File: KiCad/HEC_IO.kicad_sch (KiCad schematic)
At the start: 0 parts

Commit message: Add HEC Bus
The HEC bus packs a lot of information into a small amount of pins. It is suitable for cards with various complexity.
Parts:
- added BUS1, BUS2: ~, symbol New_Library:Bus_HEC
- added BUS3, BUS4: ~, symbol New_Library:Bus_HEC_5Vonly

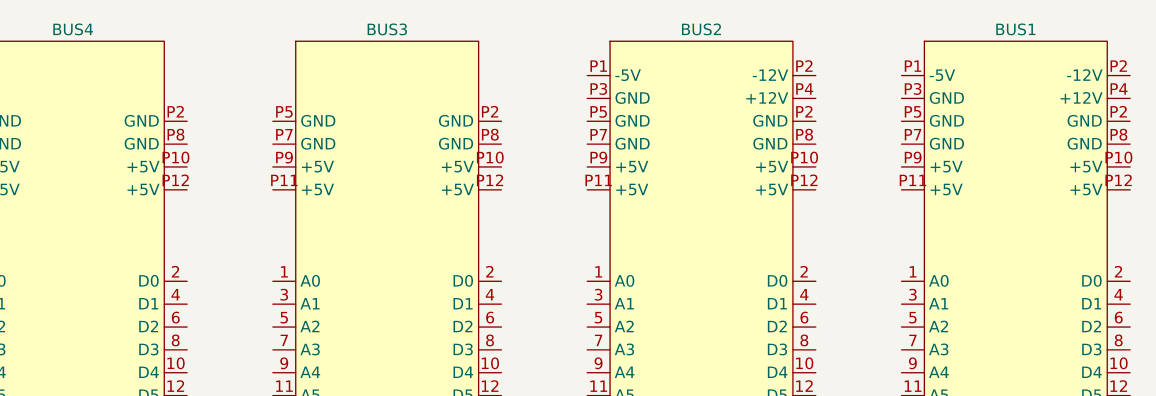
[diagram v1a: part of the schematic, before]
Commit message: Created footprint for HEC bus
Created footprints for HEC bus and some other updates.
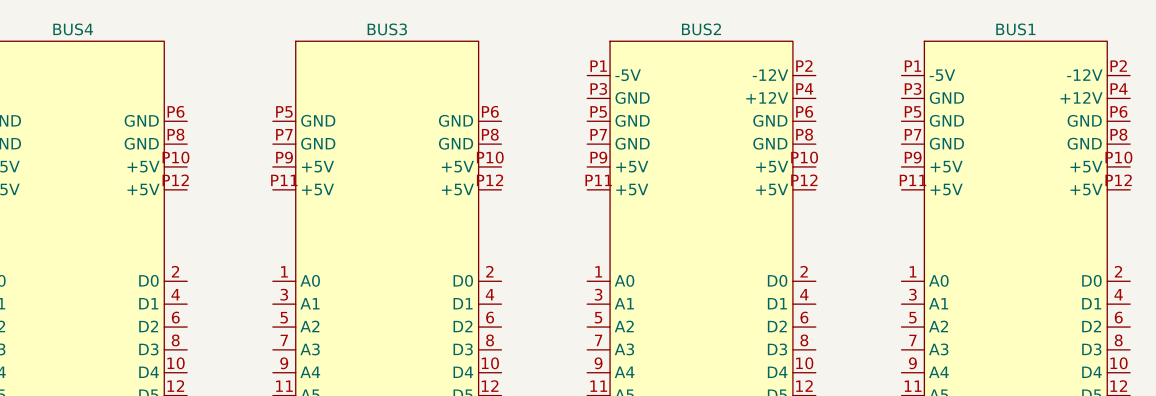
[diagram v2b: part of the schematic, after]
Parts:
- BUS1, BUS2: footprint (none) -> Library:Bus_HEC
- BUS3, BUS4: footprint (none) -> Library:Bus_HEC_5Vonly
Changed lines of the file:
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@@
       (effects (font (size 1.27 1.27)))
     )
-    (property "Footprint" "" (at 104.775 68.58 0)
+    (property "Footprint" "Library:Bus_HEC" (at 104.775 68.58 0)
       (effects (font (size 1.27 1.27)) hide)
     )
@@
     (pin "P11")
     (pin "P12")
-    (pin "P2")
     (pin "P2")
     (pin "P3")
     (pin "P4")
     (pin "P5")
+    (pin "P6")
     (pin "P7")
     (pin "P8")
@@
       (effects (font (size 1.27 1.27)))
     )
-    (property "Footprint" "" (at 34.925 68.58 0)
+    (property "Footprint" "Library:Bus_HEC_5Vonly" (at 34.925 68.58 0)
       (effects (font (size 1.27 1.27)) hide)
     )
@@
     (pin "P11")
     (pin "P12")
-    (pin "P2")
-    (pin "P5")
+    (pin "P5")
+    (pin "P6")
     (pin "P7")
     (pin "P8")
@@
     )
   )
-  (symbol (lib_id "New_Library:Bus_HEC_5Vonly") (at 69.85 68.58 0) (unit 1)
+  (symbol (lib_name "Bus_HEC_5Vonly_1") (lib_id "New_Library:Bus_HEC_5Vonly") (at 69.85 68.58 0) (unit 1)
     (in_bom yes) (on_board yes) (dnp no) (fields_autoplaced)
     (property "Reference" "BUS3" (at 69.85 30.48 0)
@@
       (effects (font (size 1.27 1.27)))
     )
-    (property "Footprint" "" (at 69.85 68.58 0)
+    (property "Footprint" "Library:Bus_HEC_5Vonly" (at 69.85 68.58 0)
       (effects (font (size 1.27 1.27)) hide)
     )
@@
     (pin "P11")
     (pin "P12")
-    (pin "P2")
-    (pin "P5")
+    (pin "P5")
+    (pin "P6")
     (pin "P7")
     (pin "P8")
@@
     )
   )
-  (symbol (lib_id "New_Library:Bus_HEC") (at 139.7 68.58 0) (unit 1)
+  (symbol (lib_name "Bus_HEC_1") (lib_id "New_Library:Bus_HEC") (at 139.7 68.58 0) (unit 1)
     (in_bom yes) (on_board yes) (dnp no) (fields_autoplaced)
     (property "Reference" "BUS1" (at 139.7 30.48 0)
@@
       (effects (font (size 1.27 1.27)))
     )
-    (property "Footprint" "" (at 139.7 68.58 0)
+    (property "Footprint" "Library:Bus_HEC" (at 139.7 68.58 0)
       (effects (font (size 1.27 1.27)) hide)
     )
@@
     (pin "P11")
     (pin "P12")
-    (pin "P2")
     (pin "P2")
     (pin "P3")
     (pin "P4")
     (pin "P5")
-    (pin "P7")
-    (pin "P8")
+    (pin "P6")
+    (pin "P7")
+    (pin "P8")

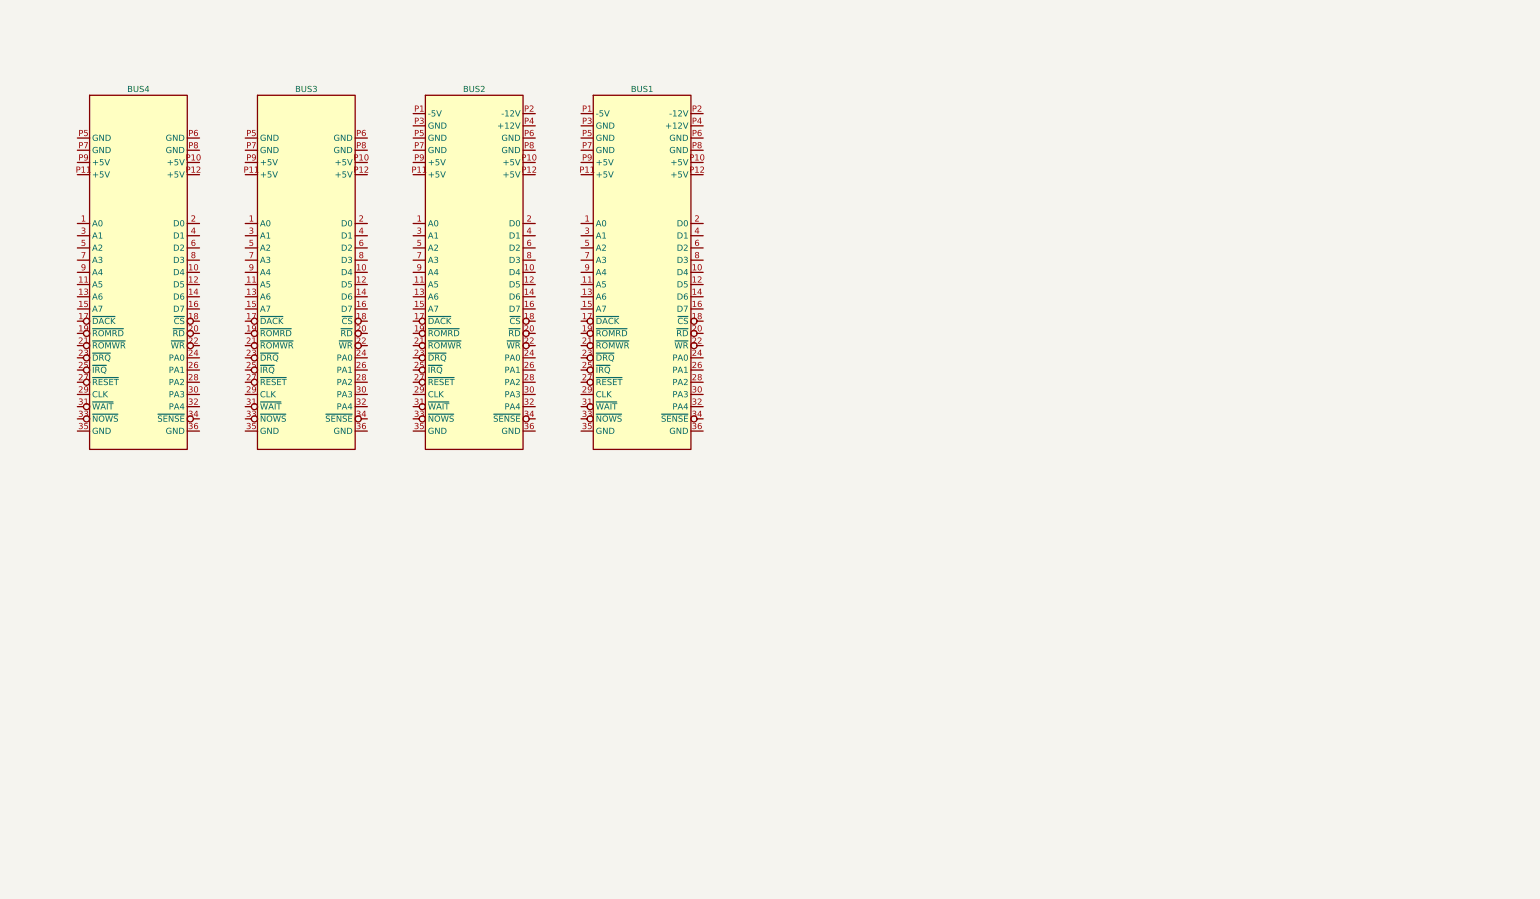
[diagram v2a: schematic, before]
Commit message: IO implementation
Implemented most of IO functions, add connections between the schematics.
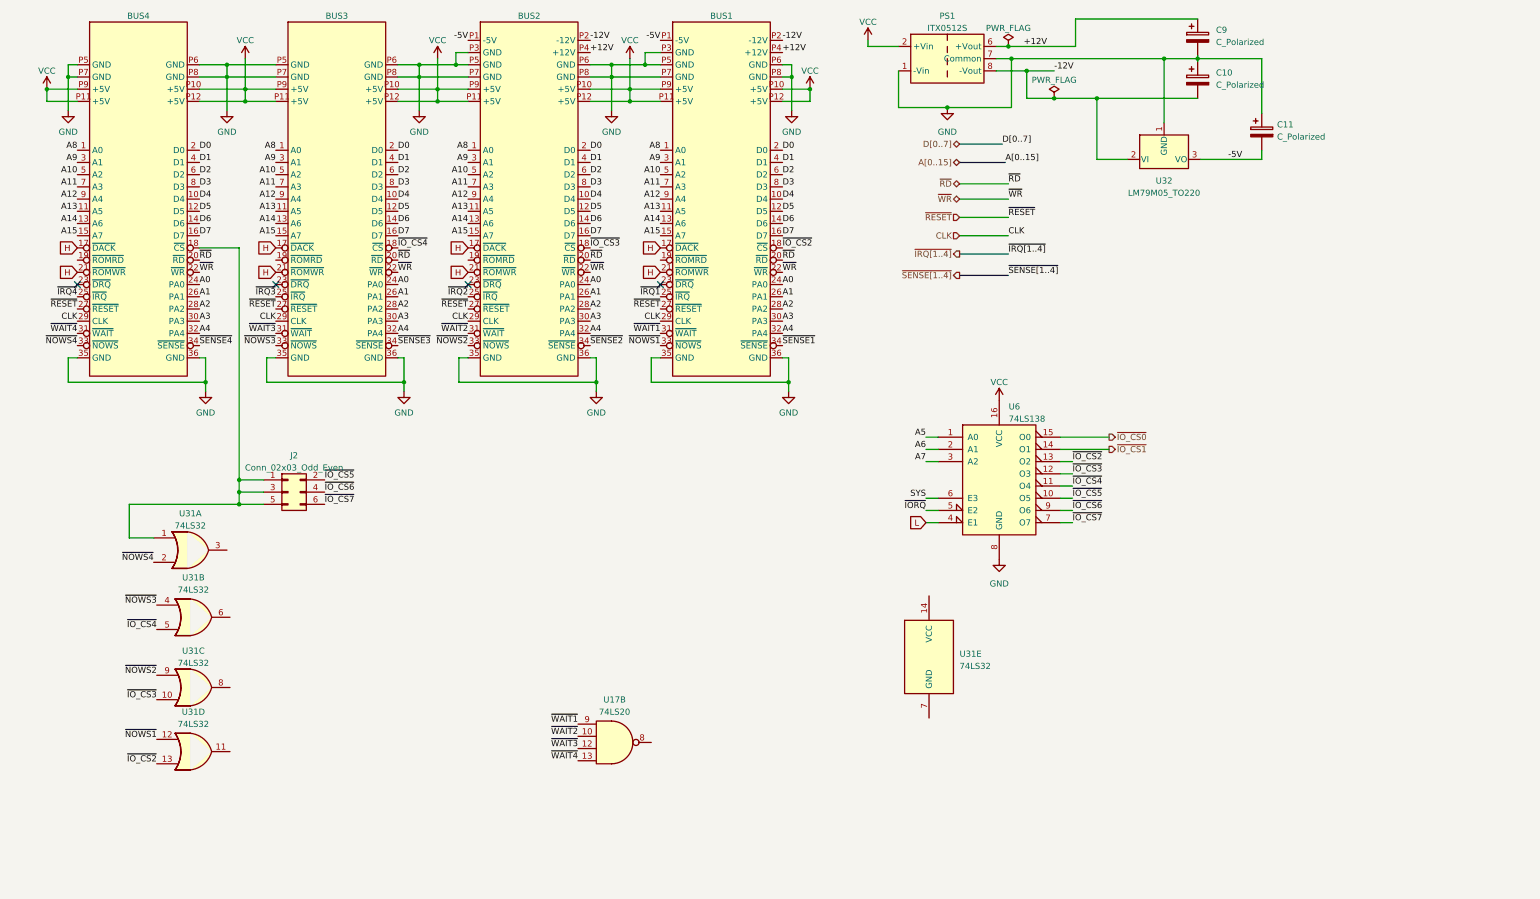
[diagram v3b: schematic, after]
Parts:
- added C10, C11, C9: C_Polarized, symbol Device:C_Polarized
- added J2: Conn_02x03_Odd_Even, symbol Connector_Generic:Conn_02x03_Odd_Even
- added PS1: ITX0512S, Converter_DCDC:Converter_DCDC_XP_POWER-ITxxxxxS_THT, symbol Converter_DCDC:ITX0512S
- added U17: 74LS20, symbol 74xx:74LS20
- added U31: 74LS32, symbol 74xx:74LS32
- added U32: LM79M05_TO220, Package_TO_SOT_THT:TO-92_Inline, symbol Regulator_Linear:LM79M05_TO220
- added U6: 74LS138, Package_DIP:DIP-16_W7.62mm_Socket, symbol 74xx:74LS138
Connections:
- net A8: now reaches BUS2.1 (A0)
- net A8: now also BUS1.1 (A0), BUS3.1 (A0), BUS4.1 (A0)
- net D4: now reaches BUS2.10 (D4)
- net D4: now also BUS1.10 (D4), BUS3.10 (D4), BUS4.10 (D4)
- net A13: now reaches BUS2.11 (A5)
- net A13: now also BUS1.11 (A5), BUS3.11 (A5), BUS4.11 (A5)
- net D5: now reaches BUS2.12 (D5)
- net D5: now also BUS1.12 (D5), BUS3.12 (D5), BUS4.12 (D5)
- net A14: now reaches BUS2.13 (A6)
- net A14: now also BUS1.13 (A6), BUS3.13 (A6), BUS4.13 (A6)
- net D6: now reaches BUS2.14 (D6)
- net D6: now also BUS1.14 (D6), BUS3.14 (D6), BUS4.14 (D6)
- net A15: now reaches BUS2.15 (A7)
- net A15: now also BUS1.15 (A7), BUS3.15 (A7), BUS4.15 (A7)
- net D7: now reaches BUS2.16 (D7)
- net D7: now also BUS1.16 (D7), BUS3.16 (D7), BUS4.16 (D7)
- net H: now reaches BUS2.17 (~{DACK})
- net H: now also BUS1.17 (~{DACK}), BUS1.21 (~{ROMWR}), BUS2.21 (~{ROMWR}), BUS3.17 (~{DACK}), BUS3.21 (~{ROMWR}), BUS4.17 (~{DACK}), BUS4.21 (~{ROMWR})
- net ~{IO_CS3}: now reaches BUS2.18 (~{CS})
- net ~{IO_CS3}: now also U31.10, U6.12 (O3)
- net D0: now reaches BUS2.2 (D0)
- net D0: now also BUS1.2 (D0), BUS3.2 (D0), BUS4.2 (D0)
- net ~{RD}: now reaches BUS2.20 (~{RD})
- net ~{RD}: now also BUS1.20 (~{RD}), BUS3.20 (~{RD}), BUS4.20 (~{RD})
- net ~{WR}: now reaches BUS2.22 (~{WR})
- net ~{WR}: now also BUS1.22 (~{WR}), BUS3.22 (~{WR}), BUS4.22 (~{WR})
- net A0: now reaches BUS2.24 (PA0)
- net A0: now also BUS1.24 (PA0), BUS3.24 (PA0), BUS4.24 (PA0)
- net ~{IRQ2}: now reaches BUS2.25 (~{IRQ})
- net A1: now reaches BUS2.26 (PA1)
- net A1: now also BUS1.26 (PA1), BUS3.26 (PA1), BUS4.26 (PA1)
- net ~{RESET}: now reaches BUS2.27 (~{RESET})
- net ~{RESET}: now also BUS1.27 (~{RESET}), BUS3.27 (~{RESET}), BUS4.27 (~{RESET})
- net A2: now reaches BUS2.28 (PA2)
- net A2: now also BUS1.28 (PA2), BUS3.28 (PA2), BUS4.28 (PA2)
- net CLK: now reaches BUS2.29 (CLK)
- net CLK: now also BUS1.29 (CLK), BUS3.29 (CLK), BUS4.29 (CLK)
- net A9: now reaches BUS2.3 (A1)
- net A9: now also BUS1.3 (A1), BUS3.3 (A1), BUS4.3 (A1)
- net A3: now reaches BUS2.30 (PA3)
- net A3: now also BUS1.30 (PA3), BUS3.30 (PA3), BUS4.30 (PA3)
- net ~{WAIT2}: now reaches BUS2.31 (~{WAIT})
- net ~{WAIT2}: now also U17.10
- net A4: now reaches BUS2.32 (PA4)
- net A4: now also BUS1.32 (PA4), BUS3.32 (PA4), BUS4.32 (PA4)
- net ~{NOWS2}: now reaches BUS2.33 (~{NOWS})
- net ~{NOWS2}: now also U31.9
- net ~{SENSE2}: now reaches BUS2.34 (~{SENSE})
- net GND: now reaches BUS2.35 (GND)
- net GND: now also BUS1.35 (GND), BUS1.36 (GND), BUS1.P3 (GND), BUS1.P5 (GND), BUS1.P6 (GND), BUS1.P7 (GND), BUS1.P8 (GND), BUS2.36 (GND), BUS2.P3 (GND), BUS2.P5 (GND), BUS2.P6 (GND), BUS2.P7 (GND), BUS2.P8 (GND), BUS3.35 (GND), BUS3.36 (GND), BUS3.P5 (GND), BUS3.P6 (GND), BUS3.P7 (GND), BUS3.P8 (GND), BUS4.35 (GND), BUS4.36 (GND), BUS4.P5 (GND), BUS4.P6 (GND), BUS4.P7 (GND), BUS4.P8 (GND), C10.1, C11.1, C9.2, PS1.1 (-Vin), PS1.7 (Common), U32.1 (GND), U6.8 (GND)
- net D1: now reaches BUS2.4 (D1)
- net D1: now also BUS1.4 (D1), BUS3.4 (D1), BUS4.4 (D1)
- net A10: now reaches BUS2.5 (A2)
- net A10: now also BUS1.5 (A2), BUS3.5 (A2), BUS4.5 (A2)
- net D2: now reaches BUS2.6 (D2)
- net D2: now also BUS1.6 (D2), BUS3.6 (D2), BUS4.6 (D2)
- net A11: now reaches BUS2.7 (A3)
- net A11: now also BUS1.7 (A3), BUS3.7 (A3), BUS4.7 (A3)
- net D3: now reaches BUS2.8 (D3)
- net D3: now also BUS1.8 (D3), BUS3.8 (D3), BUS4.8 (D3)
- net A12: now reaches BUS2.9 (A4)
- net A12: now also BUS1.9 (A4), BUS3.9 (A4), BUS4.9 (A4)
- net -5V: now reaches BUS2.P1 (-5V)
- net -5V: now also BUS1.P1 (-5V), C11.2, U32.3 (VO)
- net VCC: now reaches BUS2.P10 (+5V)
- net VCC: now also BUS1.P10 (+5V), BUS1.P11 (+5V), BUS1.P12 (+5V), BUS1.P9 (+5V), BUS2.P11 (+5V), BUS2.P12 (+5V), BUS2.P9 (+5V), BUS3.P10 (+5V), BUS3.P11 (+5V), BUS3.P12 (+5V), BUS3.P9 (+5V), BUS4.P10 (+5V), BUS4.P11 (+5V), BUS4.P12 (+5V), BUS4.P9 (+5V), PS1.2 (+Vin), U6.16 (VCC)
- net -12V: now reaches BUS2.P2 (-12V)
- net -12V: now also BUS1.P2 (-12V), C10.2, PS1.8 (-Vout), U32.2 (VI)
- net +12V: now reaches BUS2.P4 (+12V)
- net +12V: now also BUS1.P4 (+12V), C9.1, PS1.6 (+Vout)
- net at BUS4.18 (~{CS}): now also J2.1 (Pin_1), J2.3 (Pin_3), J2.5 (Pin_5), U31.1
- net ~{IRQ4}: now reaches BUS4.25 (~{IRQ})
- net ~{WAIT4}: now reaches BUS4.31 (~{WAIT})
- net ~{WAIT4}: now also U17.13
- net ~{NOWS4}: now reaches BUS4.33 (~{NOWS})
- net ~{NOWS4}: now also U31.2
- net ~{SENSE4}: now reaches BUS4.34 (~{SENSE})
- net ~{IO_CS4}: now reaches BUS3.18 (~{CS})
- net ~{IO_CS4}: now also U31.5, U6.11 (O4)
- net ~{IRQ3}: now reaches BUS3.25 (~{IRQ})
- net ~{WAIT3}: now reaches BUS3.31 (~{WAIT})
- net ~{WAIT3}: now also U17.12
- net ~{NOWS3}: now reaches BUS3.33 (~{NOWS})
- net ~{NOWS3}: now also U31.4
- net ~{SENSE3}: now reaches BUS3.34 (~{SENSE})
- net ~{IO_CS2}: now reaches BUS1.18 (~{CS})
- net ~{IO_CS2}: now also U31.13, U6.13 (O2)
- net ~{IRQ1}: now reaches BUS1.25 (~{IRQ})
- net ~{WAIT1}: now reaches BUS1.31 (~{WAIT})
- net ~{WAIT1}: now also U17.9
- net ~{NOWS1}: now reaches BUS1.33 (~{NOWS})
- net ~{NOWS1}: now also U31.12
- net ~{SENSE1}: now reaches BUS1.34 (~{SENSE})
- new net A5: U6.1 (A0)
- new net A6: U6.2 (A1)
- new net A7: U6.3 (A2)
- new net L: U6.4 (E1)
- new net SYS: U6.6 (E3)
- new net ~{IORQ}: U6.5 (E2)
- new net ~{IO_CS0}: U6.15 (O0)
- new net ~{IO_CS1}: U6.14 (O1)
- new net ~{IO_CS5}: J2.2 (Pin_2), U6.10 (O5)
- new net ~{IO_CS6}: J2.4 (Pin_4), U6.9 (O6)
- new net ~{IO_CS7}: J2.6 (Pin_6), U6.7 (O7)
- no-connect marks 0 -> 4
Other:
- moved on the sheet: BUS1, BUS2, BUS3, BUS4

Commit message: Add wait state generator
Add circuit to generate 0 to 15 wait states or use external wait input.
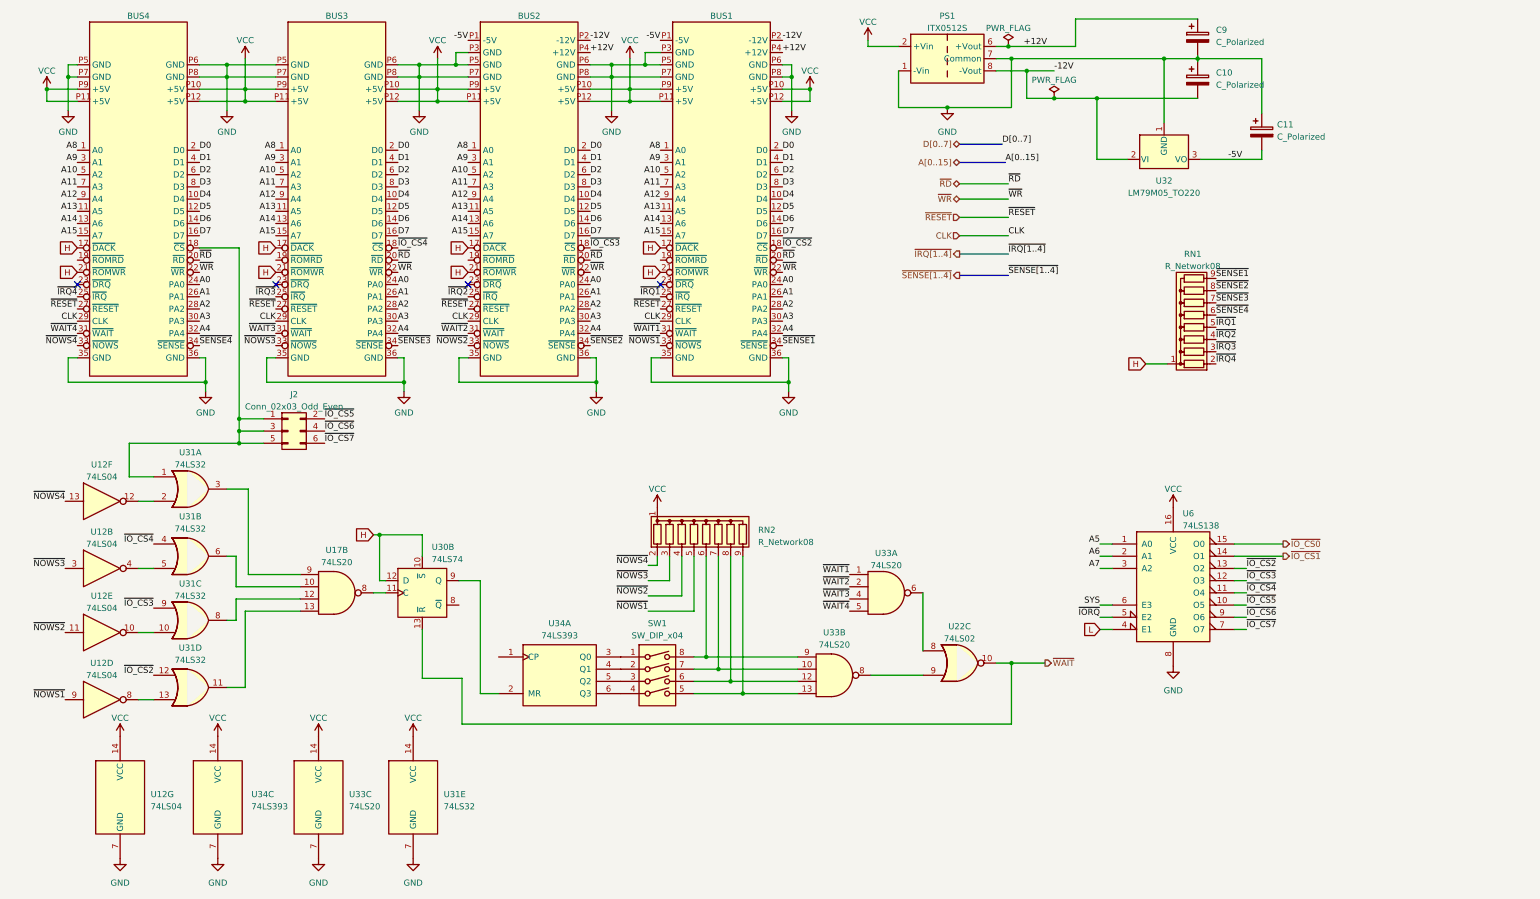
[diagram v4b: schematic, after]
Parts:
- added RN1, RN2: R_Network08, Resistor_THT:R_Array_SIP9, symbol Device:R_Network08
- added SW1: SW_DIP_x04, symbol Switch:SW_DIP_x04
- added U12: 74LS04, Package_DIP:DIP-14_W7.62mm_Socket, symbol 74xx:74LS04
- added U22: 74LS02, Package_DIP:DIP-14_W7.62mm_Socket, symbol 74xx:74LS02
- added U30: 74LS74, Package_DIP:DIP-14_W7.62mm_Socket, symbol 74xx:74LS74
- added U33: 74LS20, symbol 74xx:74LS20
- added U34: 74LS393, symbol 74xx:74LS393
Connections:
- net GND: now also U31.7 (GND), U12.7 (GND), U33.7 (GND), U34.7 (GND)
- net H: now also RN1.1 (common), U30.10 (~{S}), U30.12 (D)
- net VCC: now also U31.14 (VCC), RN2.1 (common), U12.14 (VCC), U33.14 (VCC), U34.14 (VCC)
- net ~{IO_CS2}: now also U31.12; no longer U31.13
- net ~{IO_CS3}: now also U31.9; no longer U31.10
- net ~{IO_CS4}: now also U31.4; no longer U31.5
- net ~{IRQ1}: now also RN1.5 (R4)
- net ~{IRQ2}: now also RN1.4 (R3)
- net ~{IRQ3}: now also RN1.3 (R2)
- net ~{IRQ4}: now also RN1.2 (R1)
- net ~{NOWS1}: now also RN2.5 (R4), U12.9; no longer U31.12
- net ~{NOWS2}: now also RN2.4 (R3), U12.11; no longer U31.9
- net ~{NOWS3}: now also RN2.3 (R2), U12.3; no longer U31.4
- net ~{NOWS4}: now also RN2.2 (R1), U12.13; no longer U31.2
- net ~{SENSE1}: now also RN1.9 (R8)
- net ~{SENSE2}: now also RN1.8 (R7)
- net ~{SENSE3}: now also RN1.7 (R6)
- net ~{SENSE4}: now also RN1.6 (R5)
- net ~{WAIT1}: now also U33.1; no longer U17.9
- net ~{WAIT2}: now also U33.2; no longer U17.10
- net ~{WAIT3}: now also U33.4; no longer U17.12
- net ~{WAIT4}: now also U33.5; no longer U17.13
- net at U31.3: now also U17.9
- net at U31.11: now also U17.13
- net at U17.8: now also U30.11 (C)
- net at U31.6: now also U17.10
- net at U31.8: now also U17.12
- new net: U22.8, U33.6
- new net: U22.9, U33.8
- new net: U30.9 (Q), U34.2 (MR)
- new net: SW1.1, U34.3 (Q0)
- new net: SW1.2, U34.4 (Q1)
- new net: SW1.3, U34.5 (Q2)
- new net: SW1.4, U34.6 (Q3)
- new net: U12.12, U31.2
- new net: RN2.9 (R8), SW1.5, U33.13
- new net: RN2.8 (R7), SW1.6, U33.12
- new net: RN2.7 (R6), SW1.7, U33.10
- new net: RN2.6 (R5), SW1.8, U33.9
- new net: U12.10, U31.10
- new net: U12.8, U31.13
- new net: U12.4, U31.5
- new net ~{WAIT}: U22.10, U30.13 (~{R})
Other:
- moved on the sheet: J2, U17B, U31A, U31B, U31C, U31D, U31E, U6
